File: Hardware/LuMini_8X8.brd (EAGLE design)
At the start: 25.4 x 25.4 mm, 83 parts, among them J1 LED_PADCIRCULARPAD, J2 LED_PADCIRCULARPAD, J3 LED_PADCIRCULARPAD, J4 LED_PADCIRCULARPAD, J5 LED_PADCIRCULARPAD, J6 LED_PADCIRCULARPAD, J7 LED_PADCIRCULARPAD, J8 LED_PADCIRCULARPAD

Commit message: updating repo structure
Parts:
- moved LOGO1 31.9 mm to (12.7, 14.0), flipped to the bottom
- moved U$9 2.54 mm to (23.5, 8.89)
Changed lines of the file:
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@@
 <grid distance="0.05" unitdist="inch" unit="inch" style="lines" multiple="1" display="yes" altdistance="0.005" altunitdist="inch" altunit="inch"/>
 <layers>
-<layer number="1" name="Top" color="4" fill="1" visible="yes" active="yes"/>
+<layer number="1" name="Top" color="4" fill="1" visible="no" active="yes"/>
 <layer number="2" name="Route2" color="1" fill="3" visible="no" active="no"/>
 <layer number="3" name="Route3" color="4" fill="3" visible="no" active="no"/>
@@
 <layer number="14" name="Route14" color="1" fill="6" visible="no" active="no"/>
 <layer number="15" name="Route15" color="4" fill="6" visible="no" active="no"/>
-<layer number="16" name="Bottom" color="1" fill="1" visible="yes" active="yes"/>
-<layer number="17" name="Pads" color="2" fill="1" visible="yes" active="yes"/>
-<layer number="18" name="Vias" color="2" fill="1" visible="yes" active="yes"/>
-<layer number="19" name="Unrouted" color="6" fill="1" visible="yes" active="yes"/>
+<layer number="16" name="Bottom" color="1" fill="1" visible="no" active="yes"/>
+<layer number="17" name="Pads" color="2" fill="1" visible="no" active="yes"/>
+<layer number="18" name="Vias" color="2" fill="1" visible="no" active="yes"/>
+<layer number="19" name="Unrouted" color="6" fill="1" visible="no" active="yes"/>
 <layer number="20" name="Dimension" color="15" fill="1" visible="yes" active="yes"/>
 <layer number="21" name="tPlace" color="7" fill="1" visible="yes" active="yes"/>
@@
 <layer number="49" name="Reference" color="7" fill="1" visible="yes" active="yes"/>
 <layer number="50" name="dxf" color="7" fill="1" visible="no" active="no"/>
-<layer number="51" name="tDocu" color="7" fill="1" visible="yes" active="yes"/>
+<layer number="51" name="tDocu" color="7" fill="1" visible="no" active="yes"/>
 <layer number="52" name="bDocu" color="7" fill="1" visible="yes" active="yes"/>
 <layer number="53" name="tGND_GNDA" color="7" fill="9" visible="no" active="no"/>
@@
 <element name="U$7" library="buzzard_labels (4)" package="GND6" value="" x="16.7259" y="22.098" rot="MR0"/>
 <element name="U$8" library="buzzard_labels (4)" package="GND6" value="" x="13.5255" y="3.429" rot="MR0"/>
-<element name="U$9" library="buzzard_labels (4)" package="LUMINI_8X8_MATRIX0" value="" x="23.495" y="11.43" rot="MR0"/>
+<element name="U$9" library="buzzard_labels (4)" package="LUMINI_8X8_MATRIX0" value="" x="23.495" y="8.89" rot="MR0"/>
 <element name="FRAME1" library="SparkFun-Aesthetics" package="CREATIVE_COMMONS" value="FRAME-LEDGER" x="20.32" y="-8.89">
 <attribute name="DESIGNER" value="" x="20.32" y="-8.89" size="1.778" layer="27" display="off"/>
 <attribute name="REV" value="" x="20.32" y="-8.89" size="1.778" layer="27" display="off"/>
 </element>
-<element name="LOGO1" library="SparkFun-Aesthetics" package="SFE_LOGO_NAME_FLAME_.2" value="SFE_LOGO_NAME_FLAME.2_INCH" x="10.16" y="-17.78"/>
+<element name="LOGO1" library="SparkFun-Aesthetics" package="SFE_LOGO_NAME_FLAME_.2" value="SFE_LOGO_NAME_FLAME.2_INCH" x="12.7" y="13.97" rot="MR0"/>
 </elements>
 <signals>

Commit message: pre design review
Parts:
- added C1: DNP, SparkFun-Capacitors:1206
- added H1, H2, H3, H4: STANDOFF_ELECTRICALSTANDOFF-ELECTRICAL-NOTHERMALS, SparkFun-Hardware:STANDOFF-ELECTRICAL-NOTHERMALS
- U$9: device buzzard_labels (4):LUMINI_8X8_MATRIX0 -> buzzard_labels:LUMINI_8X8_MATRIX0
- moved U$9 9.47 mm to (32.9, 10.0)
- moved D12 7.62 mm to (18.7, 4.76)
- moved D14 7.62 mm to (25.1, 4.76)
- moved D15 7.62 mm to (28.3, 4.76)
- moved D16 7.62 mm to (31.4, 4.76)
- moved D20 7.62 mm to (18.7, 7.94)
- moved D22 7.62 mm to (25.1, 7.94)
- moved D23 7.62 mm to (28.3, 7.94)
- moved D24 7.62 mm to (31.4, 7.94)
- moved D28 7.62 mm to (18.7, 11.1)
- moved D30 7.62 mm to (25.1, 11.1)
- moved D31 7.62 mm to (28.3, 11.1)
- moved D32 7.62 mm to (31.4, 11.1)
- moved D36 7.62 mm to (18.7, 14.3)
- moved D38 7.62 mm to (25.1, 14.3)
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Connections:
- net 5V: now also C1.1
- net GND: now also C1.2, H1.P1, H2.P1, H3.P1, H4.P1
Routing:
- net GND: track 8.30 -> 8.95 mm, vias 2 -> 3
- net N$61: track 25.4 -> 25.9 mm
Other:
- board size 25.4 x 25.4 mm -> 40.6 x 25.4 mm

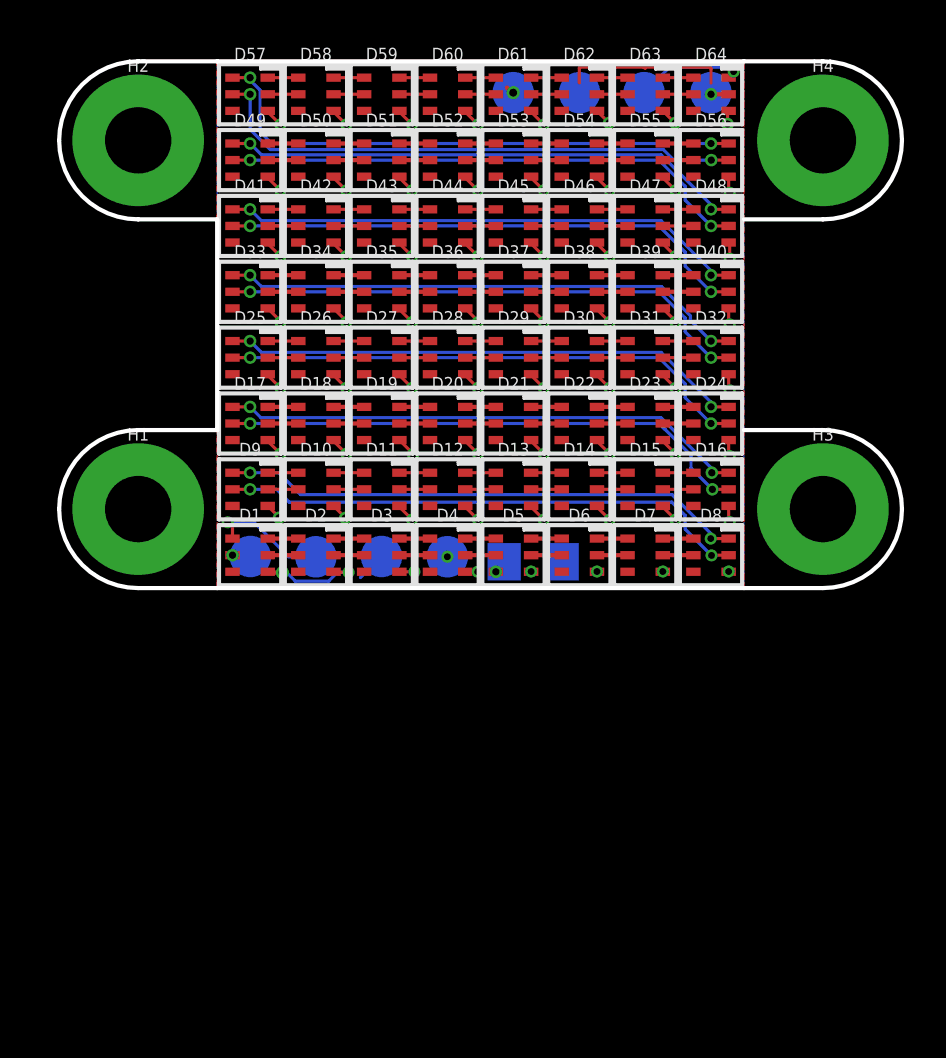
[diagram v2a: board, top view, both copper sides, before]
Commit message: updating to 4 layer
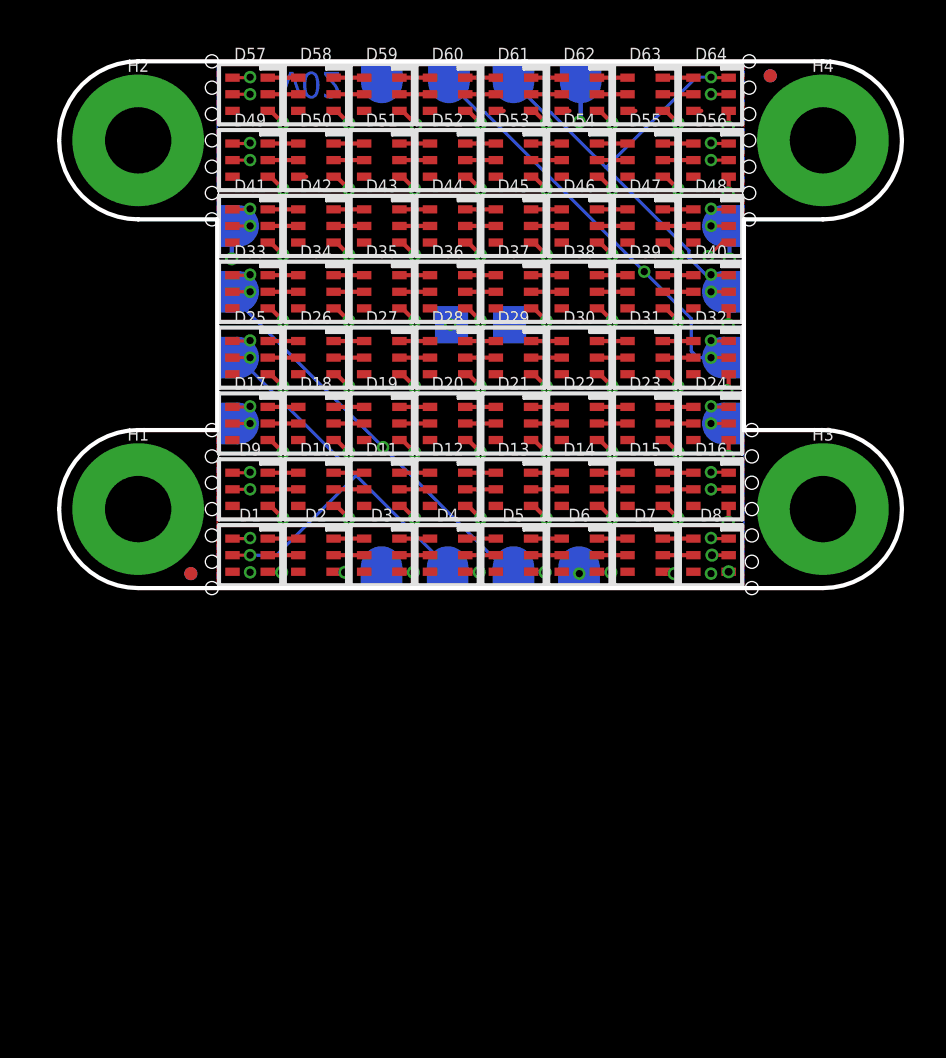
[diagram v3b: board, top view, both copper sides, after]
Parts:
- added FD1, FD2, FD3, FD4: FIDUCIALUFIDUCIAL, SparkFun-Aesthetics:FIDUCIAL-MICRO
- added J10, J11, J12, J13, J14, J15, J16, J9: LED_PAD, SparkFun-Connectors:CIRCULARPAD
- added LOGO2: OSHW-LOGOS, SparkFun-Aesthetics:OSHW-LOGO-S
- added U$10: (no value), SparkFun-Aesthetics:ORDERING_INSTRUCTIONS
- added U$11, U$18: (no value), buzzard_labels (4):5V5
- added U$12: (no value), buzzard_labels (4):CI1
- added U$13: (no value), buzzard_labels (4):DI2
- added U$14, U$15: (no value), buzzard_labels (4):GND6
- added U$16: (no value), buzzard_labels (4):DO4
- added U$17: (no value), buzzard_labels (4):CO3
- H1, H2, H3, H4: value STANDOFF_ELECTRICALSTANDOFF-ELECTRICAL-NOTHERMALS -> STANDOFF_ELECTRICAL-NOTHERMALS
- J1, J2, J3, J4, J5, J6, J7, J8: value LED_PADCIRCULARPAD -> LED_PAD; device Andy:CIRCULARPAD -> SparkFun-Connectors:CIRCULARPAD
- LOGO1: value SFE_LOGO_NAME_FLAME.2_INCH -> SFE_LOGO_NAME_FLAME.1_INCH; device SparkFun-Aesthetics:SFE_LOGO_NAME_FLAME_.2 -> SparkFun-Aesthetics:SFE_LOGO_NAME_FLAME_.1
- U$9: device buzzard_labels:LUMINI_8X8_MATRIX0 -> buzzard_labels (2):LUMINI_8X8_MATRIX0
- moved J1 27.8 mm to (8.64, 7.94), turned to 90 degrees
- moved J4 27.8 mm to (32.0, 17.5), turned to 270 degrees
- moved U$4 16.6 mm to (16.8, 22.4), turned to 180 degrees
- moved J2 16.4 mm to (32.0, 7.94), turned to 270 degrees
- moved J3 16.4 mm to (8.64, 17.5), turned to 90 degrees
- moved U$2 13.2 mm to (13.8, 22.4), turned to 180 degrees
- moved C1 11.7 mm to (20.3, 12.7)
- moved U$6 10.3 mm to (20.0, 22.4), turned to 180 degrees
- moved U$5 9.60 mm to (23.5, 2.98)
- moved J8 9.55 mm to (15.6, 24.4), turned to 180 degrees
- moved U$3 9.54 mm to (20.4, 2.98)
- moved U$8 6.43 mm to (27.6, 2.98)
- moved J7 6.37 mm to (25.1, 1.02)
- moved U$9 5.00 mm to (31.2, 5.33)
- moved LOGO1 3.81 mm to (20.3, 17.8)
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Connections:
- net 5V: now also H1.P1, H2.P1, H3.P1, H4.P1, J1.P$1, J1.P$2, J2.P$1, J2.P$2, J5.P$2, J8.P$2
- net CI: now also J10.P$1, J10.P$2, J9.P$1, J9.P$2; no longer J4.P$1
- net CO: now also J13.P$1, J13.P$2, J14.P$1, J14.P$2; no longer J1.P$1
- net DI: now also J11.P$1, J11.P$2, J12.P$1, J12.P$2; no longer J3.P$1
- net DO: now also J15.P$1, J15.P$2, J16.P$1, J16.P$2; no longer J2.P$1
- net GND: now also J3.P$1, J3.P$2, J4.P$1, J4.P$2, J6.P$2, J7.P$2; no longer H1.P1, H2.P1, H3.P1, H4.P1
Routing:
- net CO: track 0.93 -> 32.0 mm, vias 1 -> 2
- net DI: track 5.83 -> 29.4 mm, vias 1 -> 2
- net CI: track 0.89 -> 22.8 mm
- net DO: track 5.31 -> 23.2 mm
- net N$34: track 26.0 -> 30.4 mm
- net N$33: track 25.4 -> 26.8 mm
- net N$89: track 25.4 -> 26.4 mm
- net 5V: track 61.5 -> 60.5 mm
- net N$75: track 25.4 -> 26.4 mm
- net N$47: track 25.4 -> 26.3 mm
- net N$17: track 25.4 -> 26.3 mm
- net GND: track 8.95 -> 9.60 mm, vias 3 -> 7
- added copper zone on layer 2, net 5V
- added copper zone on layer 15, net GND
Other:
- outline, holes or cut-outs redrawn
- board text added: "Andy England"
- board text added: "Black PCB"
- board text added: "v02"

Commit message: changing heatsinks back to ground
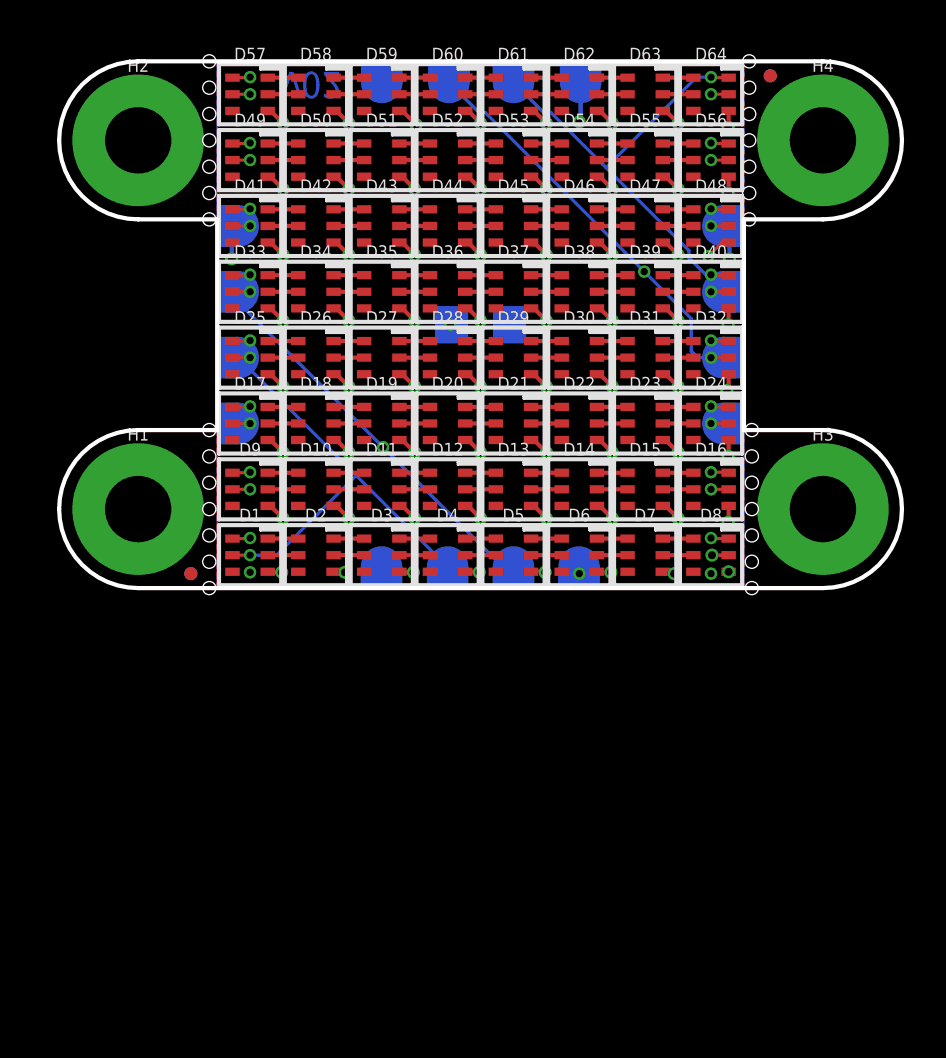
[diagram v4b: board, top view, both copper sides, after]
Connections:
- net 5V: no longer H1.P1, H2.P1, H3.P1, H4.P1
- net GND: now also H1.P1, H2.P1, H3.P1, H4.P1
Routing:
- net N$34: track 30.4 -> 26.0 mm
- net GND: track 9.60 -> 7.64 mm
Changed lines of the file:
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@@
 <grid distance="0.05" unitdist="inch" unit="inch" style="lines" multiple="1" display="yes" altdistance="0.0025" altunitdist="inch" altunit="inch"/>
 <layers>
-<layer number="1" name="Top" color="4" fill="1" visible="no" active="yes"/>
-<layer number="2" name="Route2" color="1" fill="3" visible="no" active="yes"/>
+<layer number="1" name="Top" color="4" fill="1" visible="yes" active="yes"/>
+<layer number="2" name="Route2" color="1" fill="3" visible="yes" active="yes"/>
 <layer number="3" name="Route3" color="4" fill="3" visible="no" active="no"/>
 <layer number="4" name="Route4" color="1" fill="4" visible="no" active="no"/>
@@
 <layer number="13" name="Route13" color="4" fill="5" visible="no" active="no"/>
 <layer number="14" name="Route14" color="1" fill="6" visible="no" active="no"/>
-<layer number="15" name="Route15" color="4" fill="6" visible="no" active="yes"/>
+<layer number="15" name="Route15" color="4" fill="6" visible="yes" active="yes"/>
 <layer number="16" name="Bottom" color="1" fill="1" visible="yes" active="yes"/>
 <layer number="17" name="Pads" color="2" fill="1" visible="yes" active="yes"/>
@@
 <wire x1="7.62" y1="17.78" x2="7.62" y2="7.62" width="0.2032" layer="20"/>
 <wire x1="33.02" y1="17.78" x2="33.02" y2="7.62" width="0.2032" layer="20"/>
-<hole x="7.366" y="21.59" drill="0.635"/>
-<hole x="7.366" y="22.86" drill="0.635"/>
-<hole x="7.366" y="24.13" drill="0.635"/>
-<hole x="7.366" y="25.4" drill="0.635"/>
-<hole x="7.366" y="20.32" drill="0.635"/>
-<hole x="7.366" y="19.05" drill="0.635"/>
-<hole x="7.366" y="17.78" drill="0.635"/>
-<hole x="7.366" y="3.81" drill="0.635"/>
-<hole x="7.366" y="5.08" drill="0.635"/>
-<hole x="7.366" y="6.35" drill="0.635"/>
-<hole x="7.366" y="7.62" drill="0.635"/>
-<hole x="7.366" y="2.54" drill="0.635"/>
-<hole x="7.366" y="1.27" drill="0.635"/>
-<hole x="7.366" y="0" drill="0.635"/>
+<hole x="7.239" y="21.59" drill="0.635"/>
+<hole x="7.239" y="22.86" drill="0.635"/>
+<hole x="7.239" y="24.13" drill="0.635"/>
+<hole x="7.239" y="25.4" drill="0.635"/>
+<hole x="7.239" y="20.32" drill="0.635"/>
+<hole x="7.239" y="19.05" drill="0.635"/>
+<hole x="7.239" y="17.78" drill="0.635"/>
+<hole x="7.239" y="3.81" drill="0.635"/>
+<hole x="7.239" y="5.08" drill="0.635"/>
+<hole x="7.239" y="6.35" drill="0.635"/>
+<hole x="7.239" y="7.62" drill="0.635"/>
+<hole x="7.239" y="2.54" drill="0.635"/>
+<hole x="7.239" y="1.27" drill="0.635"/>
+<hole x="7.239" y="0" drill="0.635"/>
 <hole x="33.274" y="21.59" drill="0.635"/>
 <hole x="33.274" y="22.86" drill="0.635"/>
@@
 <vertex x="33.02" y="7.62"/>
 </polygon>
-<wire x1="14.7075" y1="23.0125" x2="14.6685" y2="22.9735" width="0.2032" layer="1"/>
-<wire x1="21.0575" y1="23.0125" x2="21.4375" y2="23.0125" width="0.2032" layer="1"/>
-<wire x1="24.2325" y1="23.0125" x2="24.6125" y2="23.0125" width="0.2032" layer="1"/>
-<wire x1="27.4075" y1="23.0125" x2="27.7875" y2="23.0125" width="0.2032" layer="1"/>
-<wire x1="30.5825" y1="23.0125" x2="30.9625" y2="23.0125" width="0.2032" layer="1"/>
-<wire x1="11.5325" y1="19.8375" x2="11.9125" y2="19.8375" width="0.2032" layer="1"/>
 <polygon width="0.2032" layer="1">
 <vertex x="7.62" y="0"/>
@@
 <vertex x="7.62" y="7.62"/>
 </polygon>
+<contactref element="H4" pad="P1"/>
+<contactref element="H3" pad="P1"/>
+<contactref element="H2" pad="P1"/>
+<contactref element="H1" pad="P1"/>
 </signal>
 <signal name="5V">
@@
 <vertex x="7.62" y="17.78"/>
 </polygon>
-<contactref element="H4" pad="P1"/>
-<contactref element="H3" pad="P1"/>
-<contactref element="H2" pad="P1"/>
-<contactref element="H1" pad="P1"/>
-<wire x1="10.0575" y1="23.0125" x2="3.81" y2="21.59" width="0" layer="19" extent="1-1"/>
-<wire x1="3.81" y1="3.81" x2="8.128" y2="7.9375" width="0" layer="19" extent="16-16"/>
 </signal>
 <signal name="N$1">
@@
 <wire x1="9.2075" y1="8.763" x2="9.233" y2="8.7375" width="0.1524" layer="1"/>
 <via x="9.2075" y="8.763" extent="1-2" drill="0.35"/>
-<wire x1="28.7655" y1="5.5245" x2="29.21" y2="5.5245" width="0.1524" layer="2"/>
 <via x="31.4325" y="5.588" extent="1-2" drill="0.35"/>
 <wire x1="29.2735" y1="5.588" x2="31.4325" y2="5.588" width="0.1524" layer="2"/>
@@
 <wire x1="32.2825" y1="4.7625" x2="31.4325" y2="4.7625" width="0.1524" layer="1"/>
 <via x="31.4325" y="4.7625" extent="1-2" drill="0.35"/>
-<wire x1="31.4325" y1="4.7625" x2="26.9875" y2="4.7625" width="0.1524" layer="2"/>
 <wire x1="9.2075" y1="7.9375" x2="9.2075" y2="6.6675" width="0.1524" layer="2"/>
 <wire x1="11.1125" y1="4.7625" x2="31.4325" y2="4.7625" width="0.1524" layer="2"/>
@@
 <wire x1="9.779" y1="16.9545" x2="9.779" y2="16.0655" width="0.1524" layer="2"/>
 <wire x1="9.779" y1="16.0655" x2="10.38225" y2="15.46225" width="0.1524" layer="2"/>
-<wire x1="10.38225" y1="15.46225" x2="10.414" y2="15.4305" width="0.1524" layer="2"/>
 <wire x1="10.38225" y1="15.46225" x2="10.7315" y2="15.113" width="0.1524" layer="2"/>
 <wire x1="10.7315" y1="15.113" x2="31.4325" y2="15.113" width="0.1524" layer="2"/>
